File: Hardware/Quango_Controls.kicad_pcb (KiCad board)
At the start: 2 copper layers, 70.6 x 110 mm, 32 parts, among them J1 Conn_01x12_Male, J2 Conn_01x12_Male, J3 Conn_01x12_Male, J4 Conn_01x12_Male, J5 CV_A, J6 CV_B, J7 Out, J8 USB_C_Receptacle, J9 Midi_In, SW1 SW_Push, SW2 SW_Push

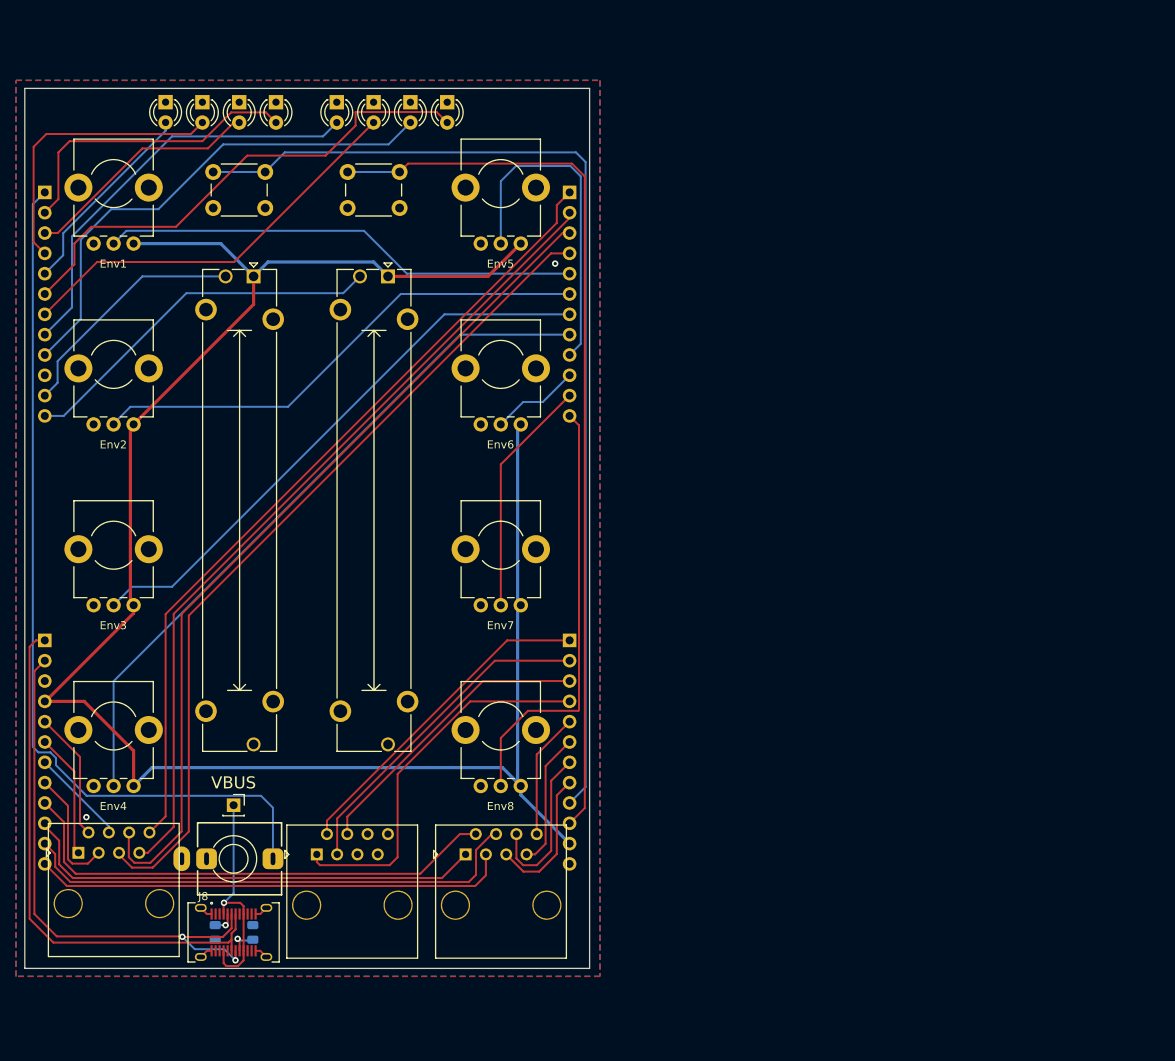
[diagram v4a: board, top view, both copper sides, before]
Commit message: Updating Controls and Panel to support gates
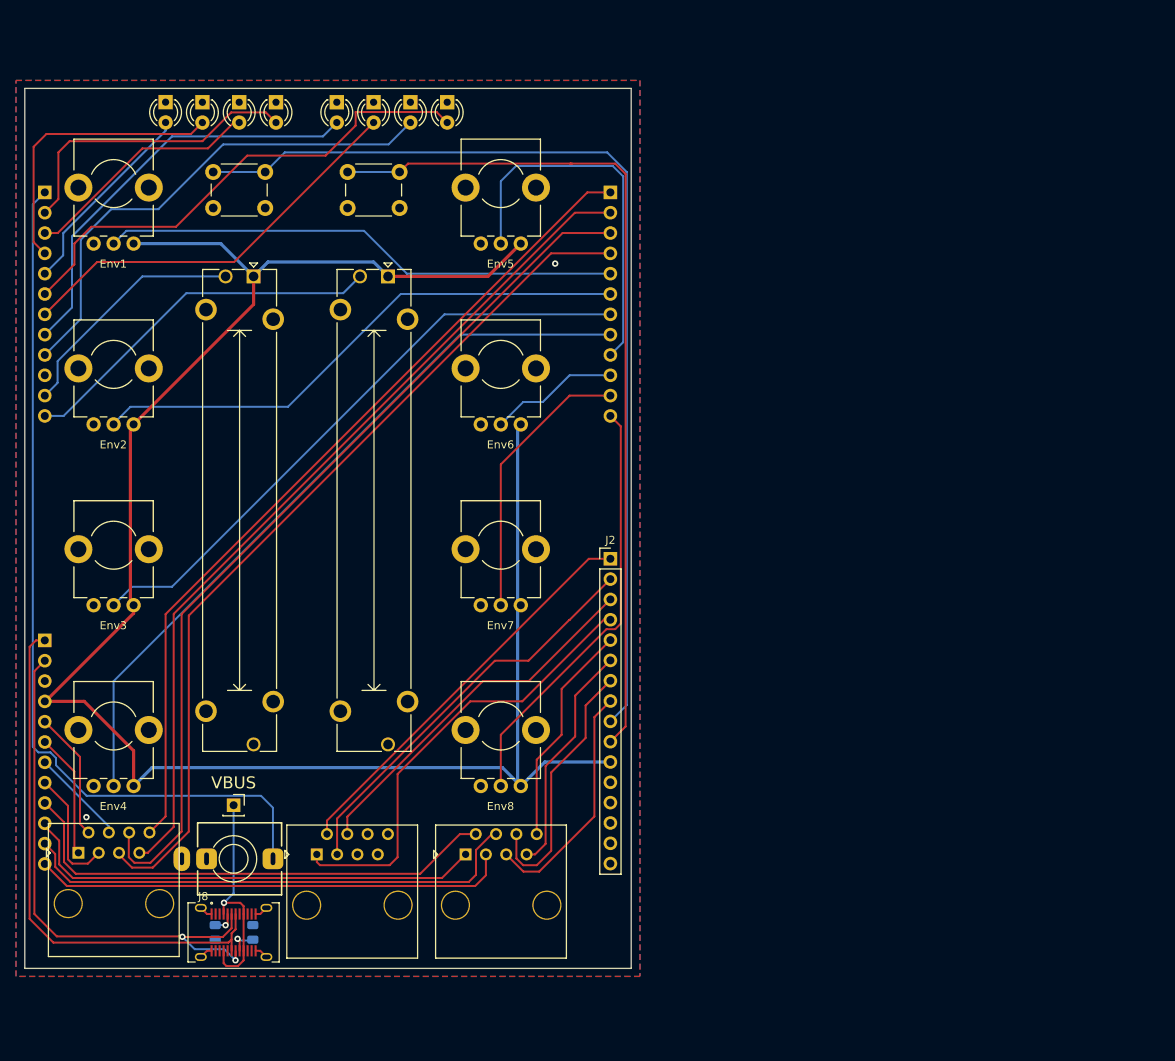
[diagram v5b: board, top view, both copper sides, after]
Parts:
- J2: value Conn_01x12_Male -> Conn_01x16_Male; footprint Connector_PinHeader_2.54mm:PinHeader_1x12_P2.54mm_Vertical -> Connector_PinHeader_2.54mm:PinHeader_1x16_P2.54mm_Vertical; moved to F.Cu
- moved J2 11.4 mm to (123.3, 97.8), turned to 0 degrees
- moved J1 5.10 mm to (123.3, 52.0)
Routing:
- net /AudioB1_In: track 17.7 -> 30.0 mm
- net /AudioB4_In: track 15.8 -> 28.1 mm
- net /AudioB3_In: track 16.9 -> 29.2 mm
- net /AudioB2_In: track 20.5 -> 32.8 mm
- net /Audio3_Out: track 41.7 -> 51.0 mm
- net /Audio1_Out: track 47.3 -> 56.6 mm
- net /Audio4_Out: track 37.0 -> 46.3 mm
- net /Audio2_Out: track 41.3 -> 50.7 mm
- net /Calib_Btn1: track 129.0 -> 123.2 mm
- net /Env2_Attack: track 42.0 -> 47.4 mm
- net /Env2_Sustain: track 29.8 -> 34.9 mm
- net /Env1_Sustain: track 72.1 -> 77.2 mm
- net /Env1_Release: track 88.0 -> 93.1 mm
- net /Env1_Decay: track 63.8 -> 68.9 mm
- net /AudioA2_In: track 107.0 -> 112.1 mm
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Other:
- board size 70.6 x 110 mm -> 75.8 x 110 mm

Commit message: Increased size to 16HP
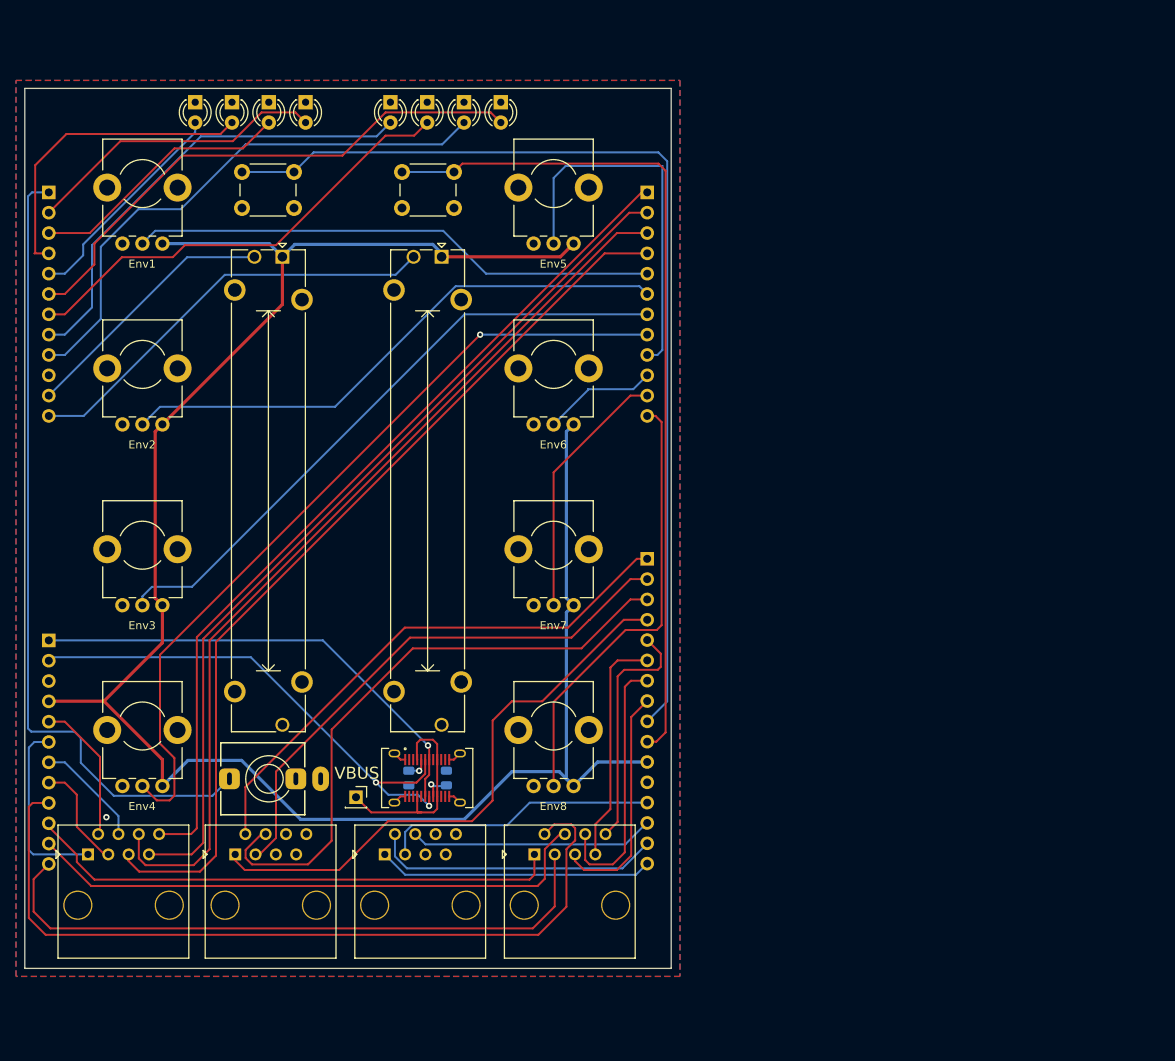
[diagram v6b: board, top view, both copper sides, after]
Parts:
- added J10: Gate_Out, Custom_Footprints:RJ45_Molex_42878-8506, F.Cu at (99.5, 139.4)
- J2: moved to B.Cu
- moved J8 31.0 mm to (100.4, 125.2)
- moved R2 31.0 mm to (102.8, 125.2)
- moved R1 31.0 mm to (98.1, 125.2)
- moved TP1 15.3 mm to (91.5, 127.6)
- moved J9 10.9 mm to (80.6, 125.3), turned to 90 degrees
- moved J7 10.2 mm to (80.8, 139.4)
- moved J6 8.60 mm to (118.2, 139.4)
- moved Level2 7.13 mm to (102.2, 60.0)
- moved SW2 6.80 mm to (100.5, 51.7)
- moved B1 6.70 mm to (95.8, 42.0)
- moved B2 6.70 mm to (100.4, 42.0)
- moved B3 6.70 mm to (105.0, 42.0)
- moved B4 6.70 mm to (109.6, 42.0)
- moved Env5 6.60 mm to (116.2, 50.9)
- moved Env6 6.60 mm to (116.2, 73.5)
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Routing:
- net /CV_OUT_B2: track 62.5 -> 100.9 mm
- net /Gate2_Out: track 0.00 -> 36.3 mm
- net /Gate3_Out: track 0.00 -> 34.6 mm
- net /Gate1_Out: track 0.00 -> 34.4 mm
- net /Gate4_Out: track 0.00 -> 30.6 mm
- net /Audio4_Out: track 46.3 -> 76.7 mm
- net /CV_OUT_B3: track 59.4 -> 80.4 mm
- net /Audio2_Out: track 50.7 -> 67.9 mm
- net /Audio3_Out: track 51.0 -> 68.1 mm
- net /Audio1_Out: track 56.6 -> 71.6 mm
- net +3.3VA: track 244.3 -> 256.5 mm
- net /MIDI_IN: track 110.0 -> 100.7 mm
- net /CV_OUT_B1: track 58.6 -> 67.2 mm
- net /USB_DM: track 67.7 -> 59.5 mm, vias 0 -> 1
- net /CV_OUT_B4: track 63.6 -> 71.6 mm
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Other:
- board size 75.8 x 110 mm -> 80.8 x 110 mm

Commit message: Added breakout for gates on component board
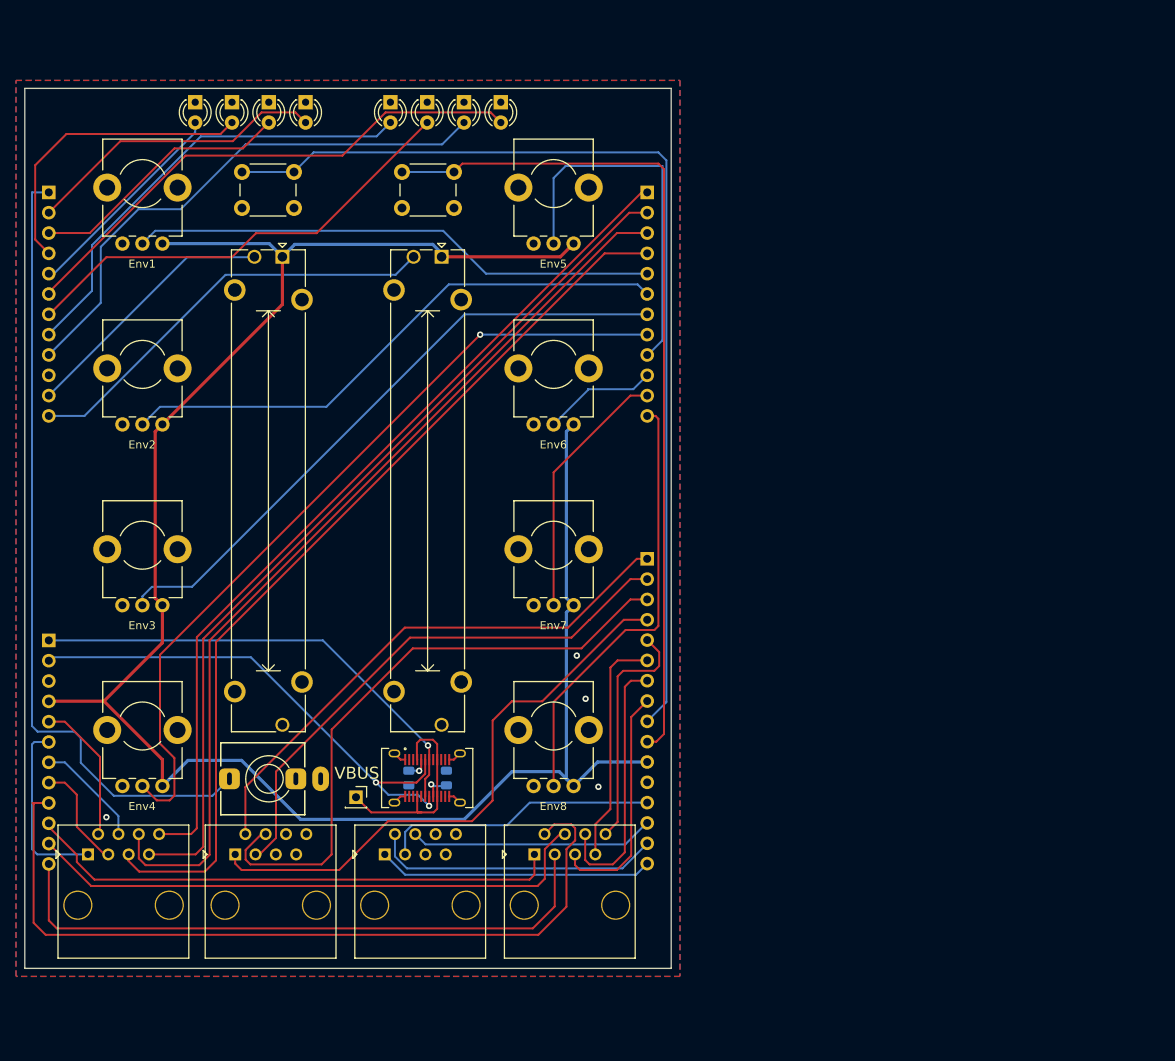
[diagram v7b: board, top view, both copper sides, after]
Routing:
- net /CV_OUT_B3: track 80.4 -> 78.4 mm
- net /EnvB4_LED_Out: track 68.0 -> 66.5 mm
- net /EnvB3_LED_Out: track 69.2 -> 68.0 mm
- net /EnvB1_LED_Out: track 58.2 -> 57.1 mm
- net /Audio4_Out: track 76.7 -> 77.8 mm
- net /EnvA2_LED_Out: track 39.6 -> 38.5 mm
- net /MIDI_IN: track 100.7 -> 99.8 mm
- net /EnvA1_LED_Out: track 27.6 -> 26.8 mm
- net /Env2_Attack: track 47.6 -> 46.9 mm
- net /CV_OUT_A1: track 23.2 -> 22.6 mm
- net /Env2_Release: track 55.5 -> 55.0 mm
- net GND: vias 1 -> 4

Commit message: Clean Up of Panel and Control boards
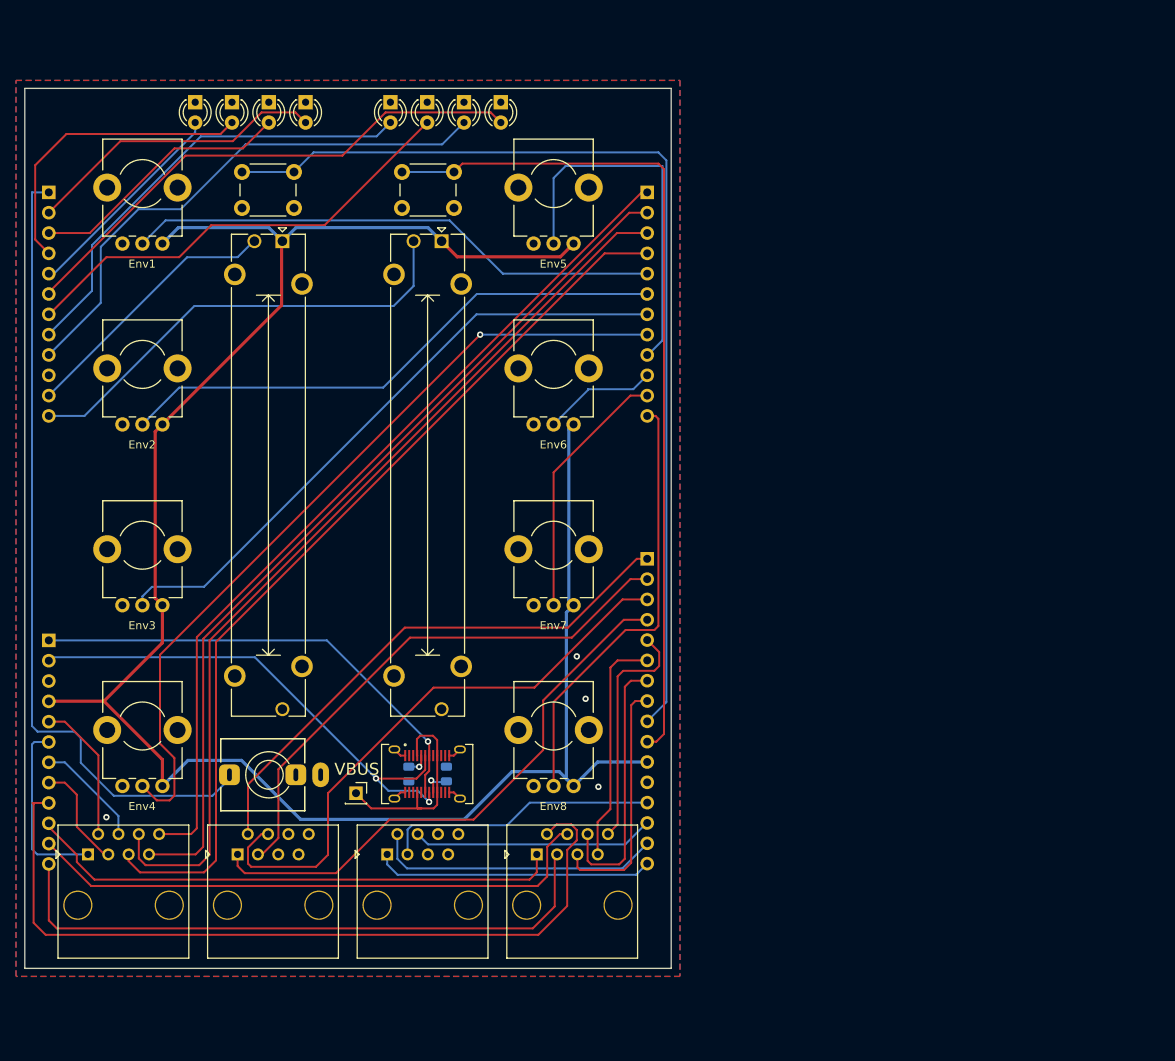
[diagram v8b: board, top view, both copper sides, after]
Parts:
- moved Level1 1.95 mm to (82.3, 58.1)
- moved Level2 1.95 mm to (102.2, 58.1)
- moved J8 0.50 mm to (100.4, 124.7)
- moved J9 0.50 mm to (80.6, 124.8)
- moved R1 0.50 mm to (98.1, 124.7)
- moved R2 0.50 mm to (102.8, 124.7)
- moved TP1 0.50 mm to (91.5, 127.1)
- moved J10 0.30 mm to (99.8, 139.4)
- moved J6 0.30 mm to (118.5, 139.4)
- moved J7 0.30 mm to (81.1, 139.4)
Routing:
- net /Audio4_Out: track 77.8 -> 73.6 mm
- net /ChannelB_Level: track 53.8 -> 57.9 mm
- net +3.3VA: track 256.5 -> 259.7 mm
- net /Audio1_Out: track 71.8 -> 69.8 mm
- net /AudioB1_In: track 29.5 -> 30.8 mm
- net /Env1_Attack: track 66.0 -> 67.1 mm
- net /Env1_Decay: track 70.8 -> 69.9 mm
- net /ChannelA_Level: track 32.9 -> 33.7 mm
- net /MIDI_IN: track 99.8 -> 100.3 mm
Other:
- board text added: "Mountjoy Modular 2023 Quango Controls v1.0"
